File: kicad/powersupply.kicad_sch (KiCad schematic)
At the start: 33 parts, among them U1 MCP602

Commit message: basic power supply
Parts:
- added C?: 100nF, symbol Device:C_Small
- added D? (x2): D_Schottky, symbol Device:D_Schottky
- added R?: 5k, Resistor_SMD:R_0603_1608Metric, symbol Device:R
- added R?: 1K, Resistor_SMD:R_0603_1608Metric, symbol Device:R
- added R?: 150, Resistor_SMD:R_0603_1608Metric, symbol Device:R
- added U? (x2): MCP602, Package_SO:SOIC-8-N7_3.9x4.9mm_P1.27mm, symbol Amplifier_Operational:LM358
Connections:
- net +3.3V: now also R?.1
- net CC: now also U?.7
- net GND: now also C?.1, D?.1 (K)
- net at R?.1, U?.7: now also R?.1; no longer Q?.2 (B)
- new net: C?.2, R?.1, U?.5 (+)
- new net: D?.2 (A), R?.2, U?.6 (-)
- new net: R?.2, U?.6 (-), U?.7
- new net: D?.1 (K), D?.2 (A)
- new net: Q?.2 (B), R?.2
- new net CC_1: U?.5 (+)
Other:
- moved on the sheet: U?

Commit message: update PDF
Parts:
- R2: value 3.3k -> 600
- RV1: value 100k -> 10k
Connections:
- net FB_(0.8v) renamed FB_(1.2v)
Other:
- moved on the sheet: Q?, R?
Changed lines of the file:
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@@
   (junction (at 50.8 66.04) (diameter 0) (color 0 0 0 0)
   )
+  (junction (at 246.38 93.98) (diameter 0) (color 0 0 0 0)
+  )
   (junction (at 151.13 40.64) (diameter 0) (color 0 0 0 0)
   )
@@
   (junction (at 195.58 26.67) (diameter 0) (color 0 0 0 0)
   )
-  (junction (at 246.38 88.9) (diameter 0) (color 0 0 0 0)
-  )
   (junction (at 175.26 119.38) (diameter 0) (color 0 0 0 0)
   )
@@
     (stroke (width 0) (type default) (color 0 0 0 0))
   )
-  (wire (pts (xy 246.38 88.9) (xy 246.38 90.17))
-    (stroke (width 0) (type default) (color 0 0 0 0))
-  )
   (wire (pts (xy 97.79 125.73) (xy 97.79 134.62))
     (stroke (width 0) (type default) (color 0 0 0 0))
@@
     (stroke (width 0) (type default) (color 0 0 0 0))
   )
-  (wire (pts (xy 252.73 88.9) (xy 246.38 88.9))
+  (wire (pts (xy 246.38 93.98) (xy 269.24 93.98))
     (stroke (width 0) (type default) (color 0 0 0 0))
   )
@@
     (stroke (width 0) (type default) (color 0 0 0 0))
   )
-  (wire (pts (xy 252.73 93.98) (xy 252.73 88.9))
-    (stroke (width 0) (type default) (color 0 0 0 0))
-  )
   (wire (pts (xy 162.56 49.53) (xy 162.56 45.72))
     (stroke (width 0) (type default) (color 0 0 0 0))
@@
     (stroke (width 0) (type default) (color 0 0 0 0))
   )
-  (wire (pts (xy 269.24 93.98) (xy 252.73 93.98))
-    (stroke (width 0) (type default) (color 0 0 0 0))
-  )
   (wire (pts (xy 135.89 44.45) (xy 138.43 44.45))
     (stroke (width 0) (type default) (color 0 0 0 0))
@@
     (stroke (width 0) (type default) (color 0 0 0 0))
   )
-  (wire (pts (xy 246.38 87.63) (xy 246.38 88.9))
-    (stroke (width 0) (type default) (color 0 0 0 0))
-  )
   (wire (pts (xy 38.1 46.99) (xy 38.1 53.34))
     (stroke (width 0) (type default) (color 0 0 0 0))
@@
     (stroke (width 0) (type default) (color 0 0 0 0))
   )
-  (wire (pts (xy 259.08 82.55) (xy 259.08 86.36))
-    (stroke (width 0) (type default) (color 0 0 0 0))
-  )
   (wire (pts (xy 243.84 33.02) (xy 245.11 33.02))
     (stroke (width 0) (type default) (color 0 0 0 0))
@@
     (stroke (width 0) (type default) (color 0 0 0 0))
   )
-  (wire (pts (xy 246.38 60.96) (xy 246.38 77.47))
+  (wire (pts (xy 246.38 60.96) (xy 246.38 83.82))
     (stroke (width 0) (type default) (color 0 0 0 0))
   )
@@
     (stroke (width 0) (type default) (color 0 0 0 0))
   )
-  (wire (pts (xy 238.76 80.01) (xy 238.76 82.55))
+  (wire (pts (xy 238.76 80.01) (xy 238.76 88.9))
     (stroke (width 0) (type default) (color 0 0 0 0))
   )
@@
   )
   (wire (pts (xy 195.58 48.26) (xy 195.58 50.8))
-    (stroke (width 0) (type default) (color 0 0 0 0))
-  )
-  (wire (pts (xy 246.38 97.79) (xy 246.38 101.6))
     (stroke (width 0) (type default) (color 0 0 0 0))
   )
@@
     (effects (font (size 3 3)) (justify left bottom))
   )
-  (global_label "FB_(0.8v)" (shape input) (at 96.52 80.01 0) (fields_autoplaced)
+  (global_label "FB_(1.2v)" (shape input) (at 96.52 80.01 0) (fields_autoplaced)
     (effects (font (size 1.27 1.27)) (justify left))
     (property "Intersheet References" "${INTERSHEET_REFS}" (id 0) (at 107.9441 79.9306 0)
@@
     )
   )
-  (global_label "FB_(0.8v)" (shape input) (at 217.17 43.18 0) (fields_autoplaced)
+  (global_label "FB_(1.2v)" (shape input) (at 217.17 43.18 0) (fields_autoplaced)
     (effects (font (size 1.27 1.27)) (justify left))
     (property "Intersheet References" "${INTERSHEET_REFS}" (id 0) (at 228.5941 43.1006 0)
@@
     (pin "2")
   )
-  (symbol (lib_id "Transistor_FET:AO3401A") (at 243.84 82.55 0) (unit 1)
-    (in_bom yes) (on_board yes) (fields_autoplaced)
-    (property "Reference" "Q?" (id 0) (at 250.19 81.2799 0)
-      (effects (font (size 1.27 1.27)) (justify left))
-    )
-    (property "Value" "AO3401A" (id 1) (at 250.19 83.8199 0)
-      (effects (font (size 1.27 1.27)) (justify left))
-    )
-    (property "Footprint" "Package_TO_SOT_SMD:SOT-23" (id 2) (at 248.92 84.455 0)
+  (symbol (lib_id "Transistor_FET:AO3401A") (at 243.84 88.9 0) (unit 1)
+    (in_bom yes) (on_board yes) (fields_autoplaced)
+    (property "Reference" "Q?" (id 0) (at 250.19 87.6299 0)
+      (effects (font (size 1.27 1.27)) (justify left))
+    )
+    (property "Value" "AO3401A" (id 1) (at 250.19 90.1699 0)
+      (effects (font (size 1.27 1.27)) (justify left))
+    )
+    (property "Footprint" "Package_TO_SOT_SMD:SOT-23" (id 2) (at 248.92 90.805 0)
       (effects (font (size 1.27 1.27) italic) (justify left) hide)
     )
-    (property "Datasheet" "http://www.aosmd.com/pdfs/datasheet/AO3401A.pdf" (id 3) (at 243.84 82.55 0)
+    (property "Datasheet" "http://www.aosmd.com/pdfs/datasheet/AO3401A.pdf" (id 3) (at 243.84 88.9 0)
       (effects (font (size 1.27 1.27)) (justify left) hide)
     )
@@
     (pin "2")
   )
-  (symbol (lib_id "Device:R") (at 246.38 93.98 0) (unit 1)
-    (in_bom yes) (on_board yes) (fields_autoplaced)
-    (property "Reference" "R?" (id 0) (at 248.92 92.7099 0)
-      (effects (font (size 1.27 1.27)) (justify left))
-    )
-    (property "Value" "1k" (id 1) (at 248.92 95.2499 0)
-      (effects (font (size 1.27 1.27)) (justify left))
-    )
-    (property "Footprint" "" (id 2) (at 244.602 93.98 90)
-      (effects (font (size 1.27 1.27)) hide)
-    )
-    (property "Datasheet" "~" (id 3) (at 246.38 93.98 0)
+  (symbol (lib_id "Device:R") (at 246.38 97.79 0) (unit 1)
+    (in_bom yes) (on_board yes) (fields_autoplaced)
+    (property "Reference" "R?" (id 0) (at 248.92 96.5199 0)
+      (effects (font (size 1.27 1.27)) (justify left))
+    )
+    (property "Value" "1k" (id 1) (at 248.92 99.0599 0)
+      (effects (font (size 1.27 1.27)) (justify left))
+    )
+    (property "Footprint" "" (id 2) (at 244.602 97.79 90)
+      (effects (font (size 1.27 1.27)) hide)
+    )
+    (property "Datasheet" "~" (id 3) (at 246.38 97.79 0)
       (effects (font (size 1.27 1.27)) hide)
     )
@@
   )
   (symbol (lib_id "power:GND") (at 246.38 101.6 0) (unit 1)
-    (in_bom yes) (on_board yes) (fields_autoplaced)
+    (in_bom yes) (on_board yes)
     (property "Reference" "#PWR?" (id 0) (at 246.38 107.95 0)
       (effects (font (size 1.27 1.27)) hide)
     )
-    (property "Value" "GND" (id 1) (at 246.38 106.68 0))
+    (property "Value" "GND" (id 1) (at 250.19 105.41 0))
     (property "Footprint" "" (id 2) (at 246.38 101.6 0)
       (effects (font (size 1.27 1.27)) hide)
@@
       (effects (font (size 1.27 1.27)) (justify right))
     )
-    (property "Value" "100k" (id 1) (at 88.9 74.9299 0)
+    (property "Value" "10k" (id 1) (at 88.9 74.9299 0)
       (effects (font (size 1.27 1.27)) (justify right))
     )
@@
       (effects (font (size 1.27 1.27)) (justify left))
     )
-    (property "Value" "3.3k" (id 1) (at 88.9 85.0899 0)
+    (property "Value" "600" (id 1) (at 88.9 85.0899 0)
       (effects (font (size 1.27 1.27)) (justify left))
     )
@@
     (pin "2")
   )
-  (symbol (lib_id "power:GND") (at 259.08 86.36 0) (unit 1)
-    (in_bom yes) (on_board yes) (fields_autoplaced)
-    (property "Reference" "#PWR?" (id 0) (at 259.08 92.71 0)
-      (effects (font (size 1.27 1.27)) hide)
-    )
-    (property "Value" "GND" (id 1) (at 259.08 91.44 0))
-    (property "Footprint" "" (id 2) (at 259.08 86.36 0)
-      (effects (font (size 1.27 1.27)) hide)
-    )
-    (property "Datasheet" "" (id 3) (at 259.08 86.36 0)
+  (symbol (lib_id "power:GND") (at 259.08 82.55 0) (unit 1)
+    (in_bom yes) (on_board yes)
+    (property "Reference" "#PWR?" (id 0) (at 259.08 88.9 0)
+      (effects (font (size 1.27 1.27)) hide)
+    )
+    (property "Value" "GND" (id 1) (at 262.89 85.09 0))
+    (property "Footprint" "" (id 2) (at 259.08 82.55 0)
+      (effects (font (size 1.27 1.27)) hide)
+    )
+    (property "Datasheet" "" (id 3) (at 259.08 82.55 0)
       (effects (font (size 1.27 1.27)) hide)
     )
@@
     )
     (path "/ff10014a-55b7-46dd-b5ca-00e8d5db1c48"
-      (reference "R2") (unit 1) (value "3.3k") (footprint "Resistor_SMD:R_0603_1608Metric")
+      (reference "R2") (unit 1) (value "600") (footprint "Resistor_SMD:R_0603_1608Metric")
     )
     (path "/b8868937-87ea-4269-aeb3-3624e53fe6a3"
@@
     )
     (path "/addbc721-31a7-4af8-8615-bd1792eeddbf"
-      (reference "RV1") (unit 1) (value "100k") (footprint "Resistor_SMD:R_0603_1608Metric")
+      (reference "RV1") (unit 1) (value "10k") (footprint "Resistor_SMD:R_0603_1608Metric")
     )
     (path "/6396ff55-ef48-45c2-8523-130f080f5e37"

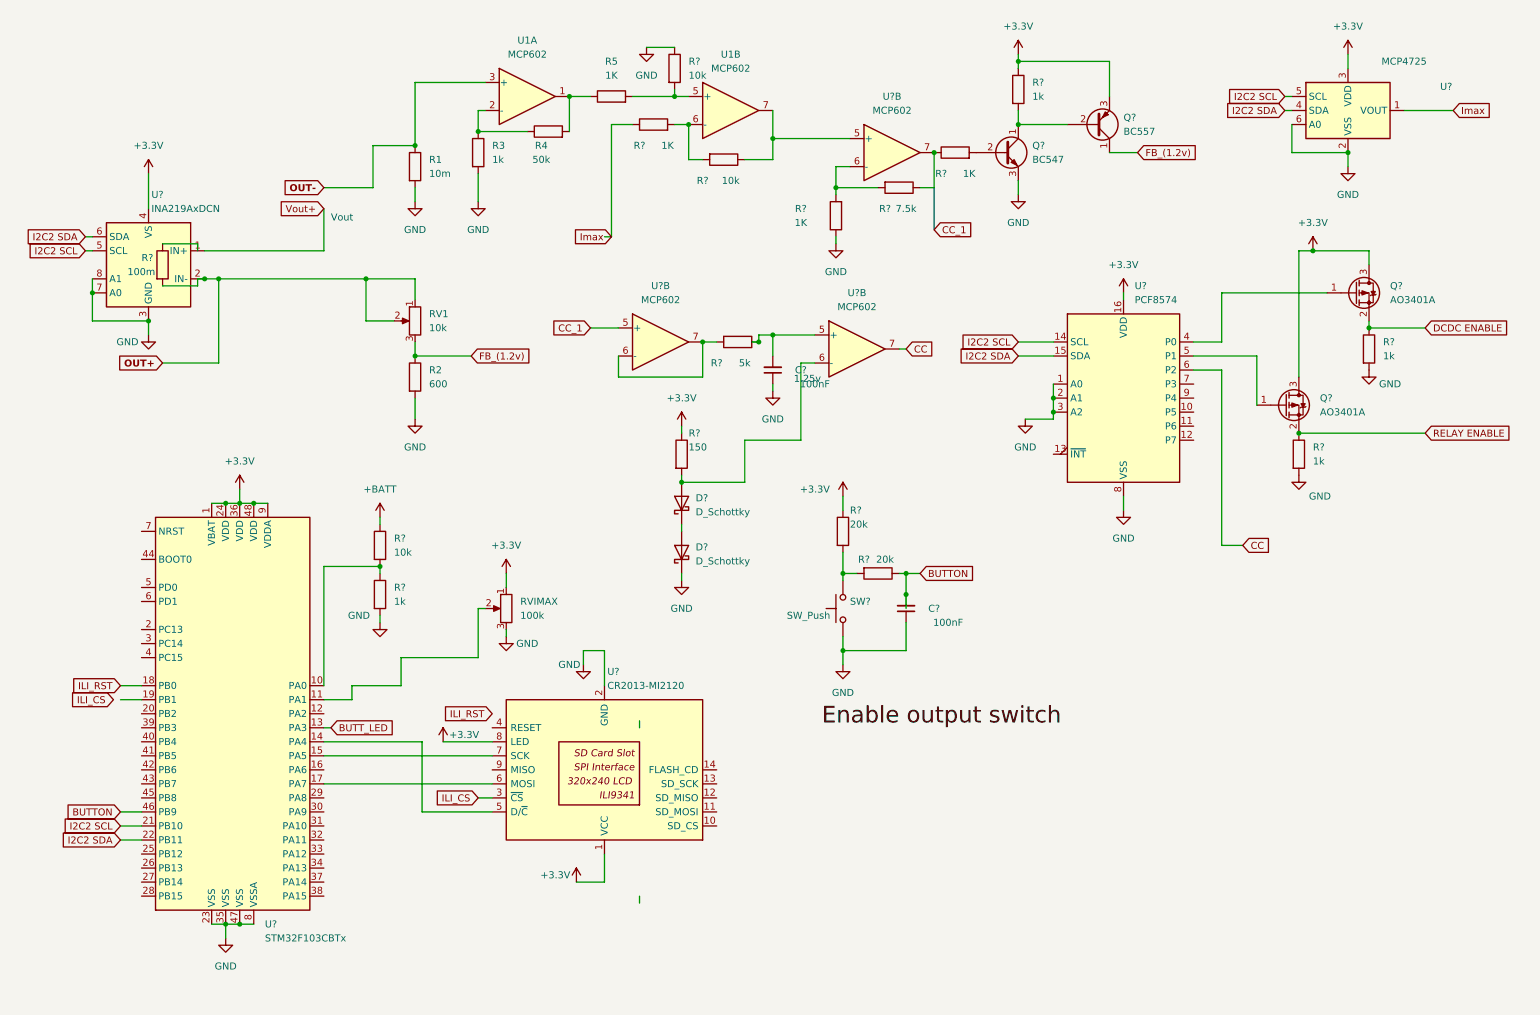
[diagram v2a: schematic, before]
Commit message: annotate components
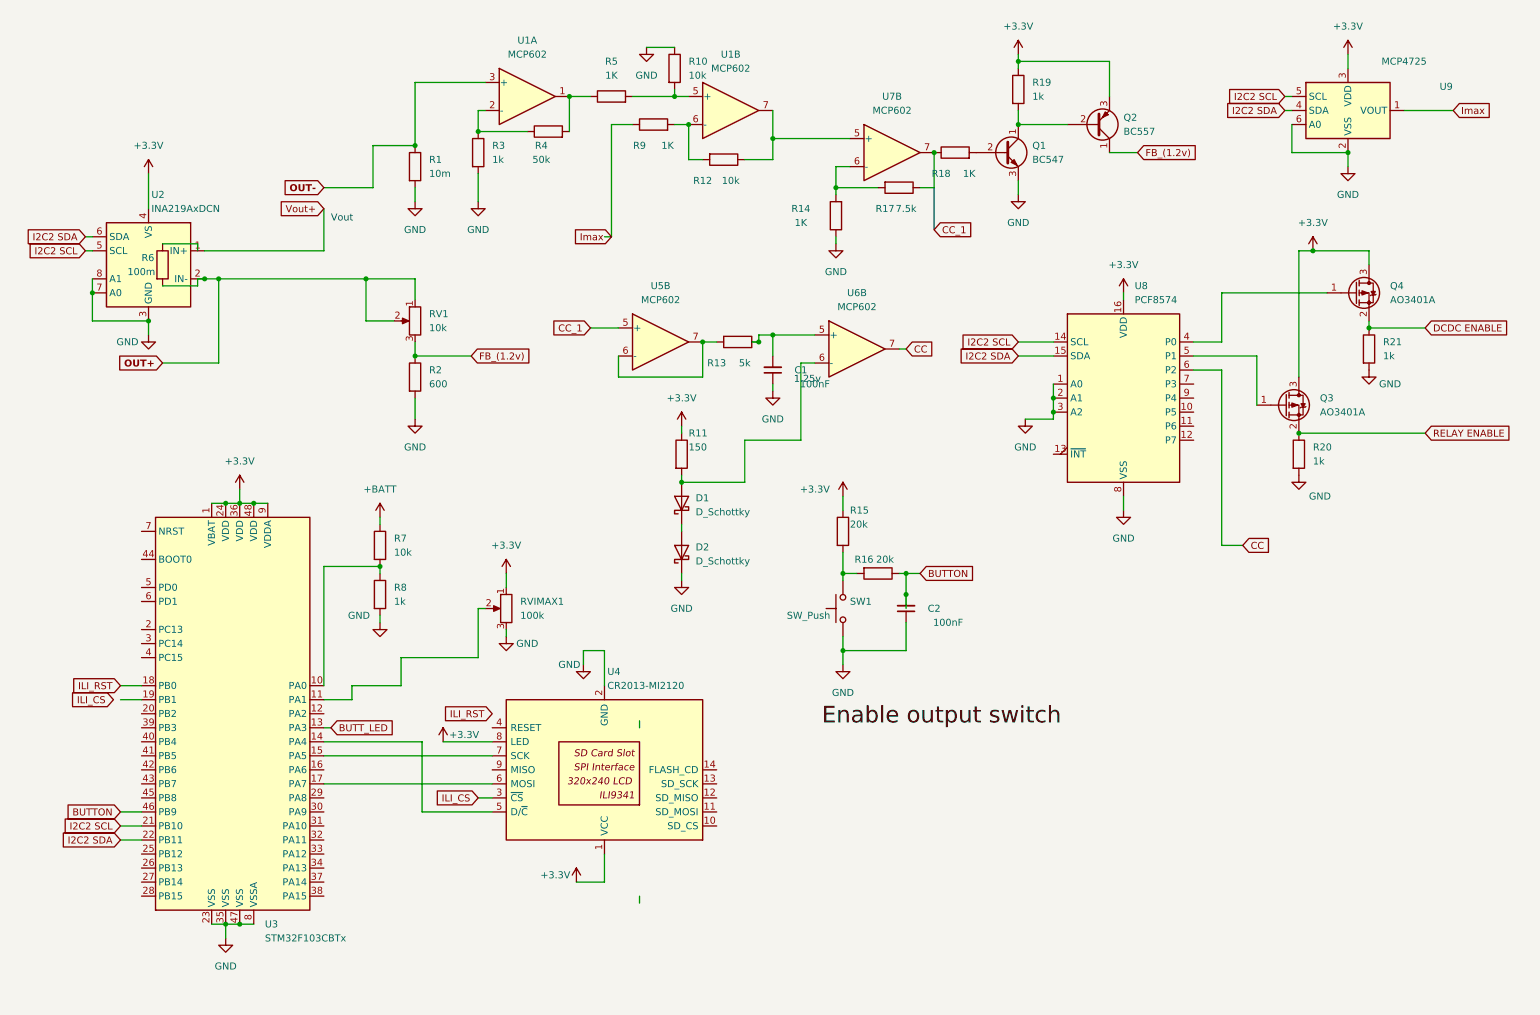
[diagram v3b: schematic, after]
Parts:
- gave numbers to parts that had none: 33
- renumbered RVIMAX to RVIMAX1

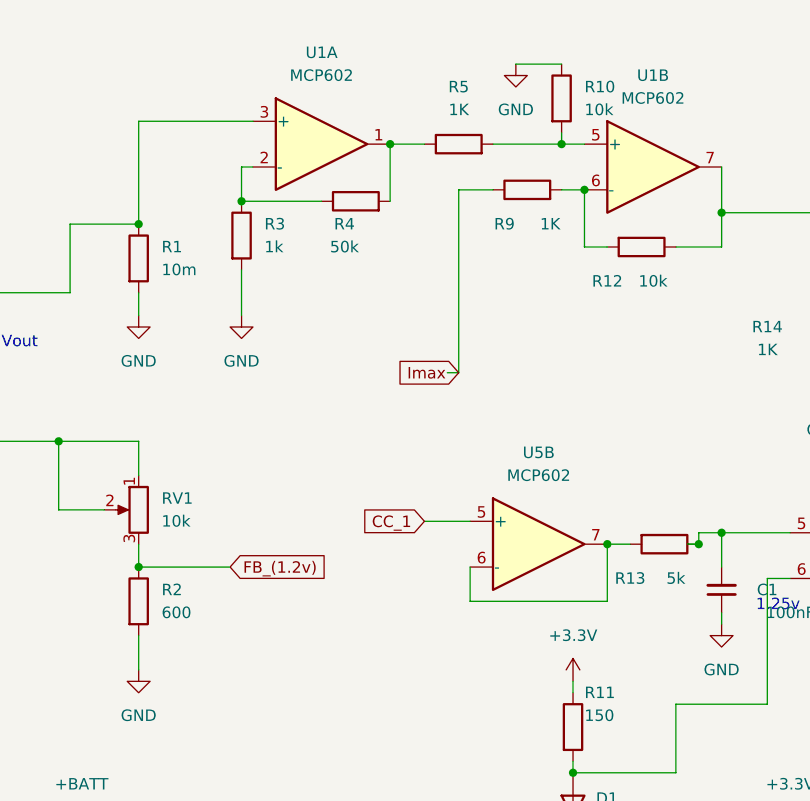
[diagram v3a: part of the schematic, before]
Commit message: by default rust is disabled + update kicad
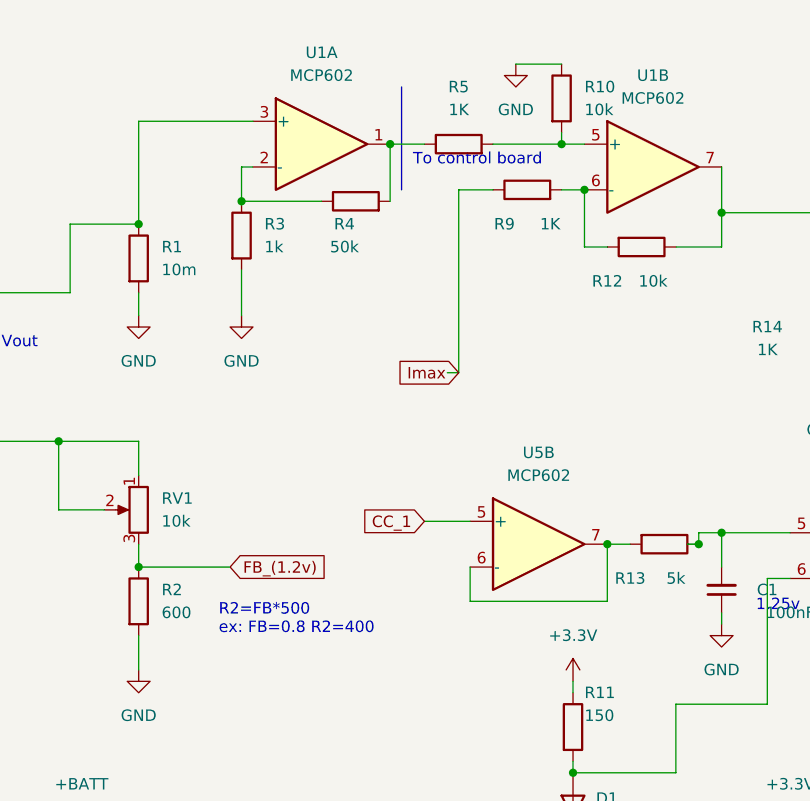
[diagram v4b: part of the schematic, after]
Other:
- note added: "R2=FB*500 ex: FB=0.8 R2=400"
- note added: "To control board"
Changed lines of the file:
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@@
+    (stroke (width 0) (type default) (color 0 0 0 0))
+  )
+  (polyline (pts (xy 115.57 26.67) (xy 115.57 38.1))
     (stroke (width 0) (type default) (color 0 0 0 0))
   )
@@
     (stroke (width 0) (type default) (color 0 0 0 0))
   )
+  (text "R2=FB*500\nex: FB=0.8 R2=400" (at 95.25 87.63 0)
+    (effects (font (size 1.27 1.27)) (justify left bottom))
+  )
+  (text "To control board\n" (at 116.84 35.56 0)
+    (effects (font (size 1.27 1.27)) (justify left bottom))
+  )
   (text "1.25v" (at 154.94 85.09 0)

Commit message: update kicad
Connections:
- net UART_TX: now reaches U3.12 (PA2)
